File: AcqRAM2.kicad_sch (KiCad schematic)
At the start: 17 parts, among them U30 MSM5416283, U31 MSM5416283, U32 MSM5416283, U33 MSM5416283, U39 MSM5416283, U40 MSM5416283, U41 MSM5416283, U42 MSM5416283, U43 MSM5416283, U50 MSM5416283, U51 MSM5416283, U52 MSM5416283, U53 MSM5416283, U58 MSM5416283, U59 MSM5416283, U60 MSM5416283, U61 MSM5416283

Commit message: complete outer layers
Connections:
- net VSC13: now reaches U60.64 (SC)
- net VSC13: now also U52.64 (SC)
- net VSC12: now reaches U41.64 (SC)
- net VSC12: now also U31.64 (SC)
- net VSC9: now reaches U50.64 (SC)
- net VSC9: now also U58.64 (SC)
- net VSC10: now reaches U51.64 (SC)
- net VSC10: now also U59.64 (SC)
- net VSC17: now reaches U39.64 (SC)
- net VSC16: now reaches U43.64 (SC)
- net VSC16: now also U33.64 (SC)
- net VSC15: now reaches U42.64 (SC)
- net VSC15: now also U32.64 (SC)
- net VSC14: now reaches U53.64 (SC)
- net VSC14: now also U61.64 (SC)
- net VSC11: now reaches U30.64 (SC)
- net VSC11: now also U40.64 (SC)
- no-connect marks 0 -> 16
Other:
- note removed: "all chips"

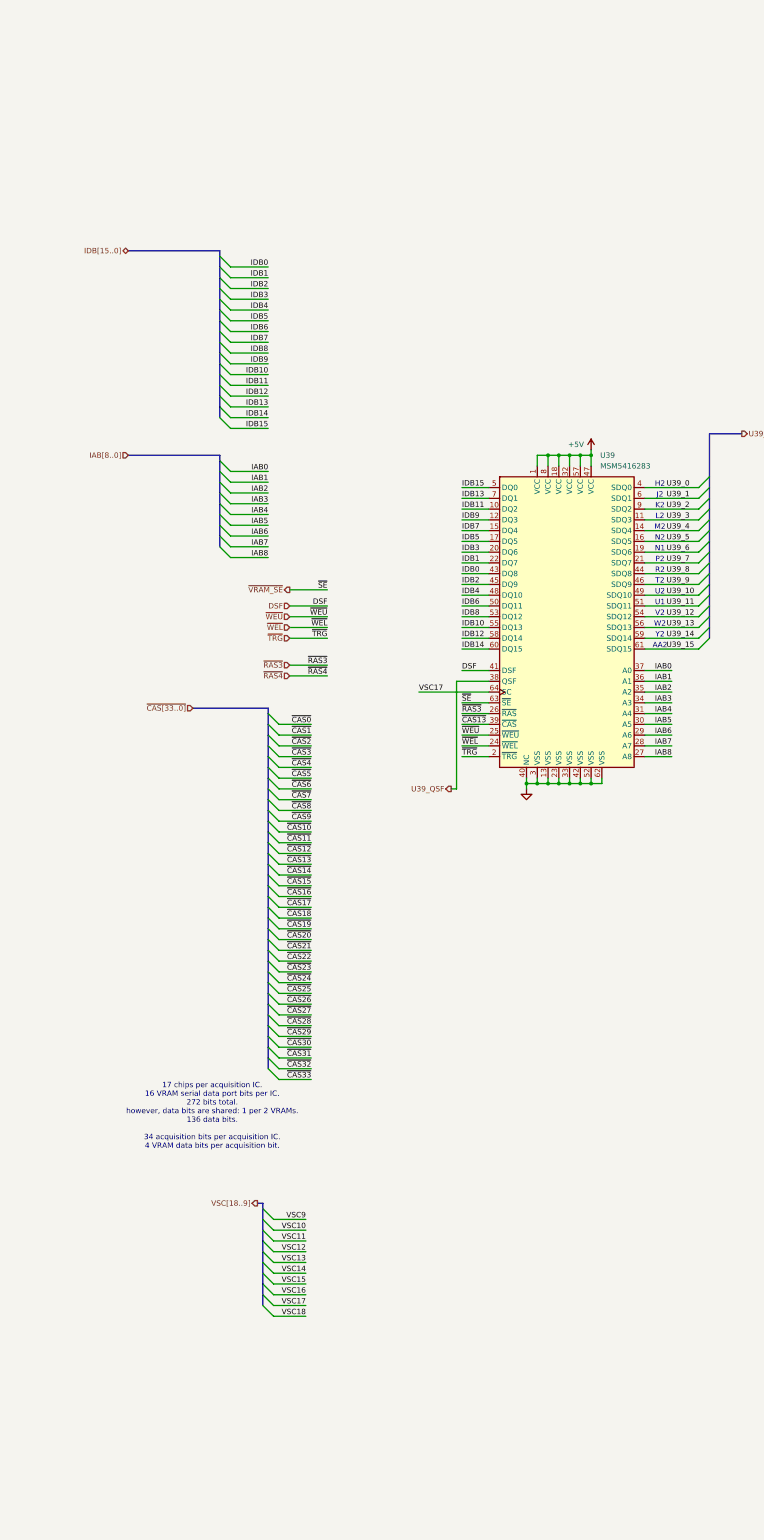
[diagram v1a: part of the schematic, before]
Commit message: add test points
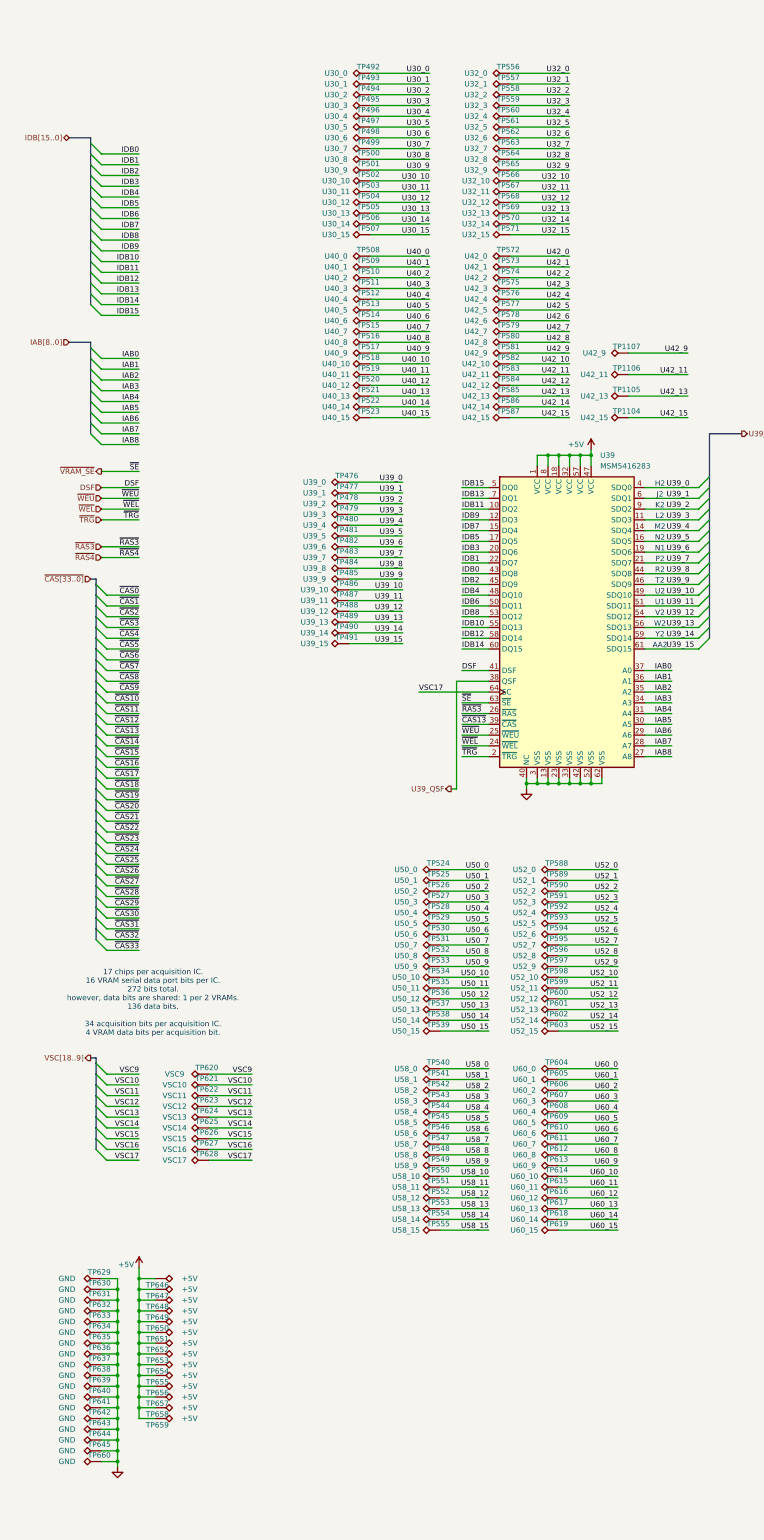
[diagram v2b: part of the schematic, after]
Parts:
- added TP1104, TP587: U42_15, hp16717:HP_TP30, symbol Connector:TestPoint_Alt
- added TP1105, TP585: U42_13, hp16717:HP_TP30, symbol Connector:TestPoint_Alt
- added TP1106, TP583: U42_11, hp16717:HP_TP30, symbol Connector:TestPoint_Alt
- added TP1107, TP581: U42_9, hp16717:HP_TP30, symbol Connector:TestPoint_Alt
- added TP476: U39_0, hp16717:HP_TP30, symbol Connector:TestPoint_Alt
- added TP477: U39_1, hp16717:HP_TP30, symbol Connector:TestPoint_Alt
- added TP478: U39_2, hp16717:HP_TP30, symbol Connector:TestPoint_Alt
- added TP479: U39_3, hp16717:HP_TP30, symbol Connector:TestPoint_Alt
- added TP480: U39_4, hp16717:HP_TP30, symbol Connector:TestPoint_Alt
- added TP481: U39_5, hp16717:HP_TP30, symbol Connector:TestPoint_Alt
- added TP482: U39_6, hp16717:HP_TP30, symbol Connector:TestPoint_Alt
- added TP483: U39_7, hp16717:HP_TP30, symbol Connector:TestPoint_Alt
- added TP484: U39_8, hp16717:HP_TP30, symbol Connector:TestPoint_Alt
- added TP485: U39_9, hp16717:HP_TP30, symbol Connector:TestPoint_Alt
- added TP486: U39_10, hp16717:HP_TP30, symbol Connector:TestPoint_Alt
- added TP487: U39_11, hp16717:HP_TP30, symbol Connector:TestPoint_Alt
- added TP488: U39_12, hp16717:HP_TP30, symbol Connector:TestPoint_Alt
- added TP489: U39_13, hp16717:HP_TP30, symbol Connector:TestPoint_Alt
- added TP490: U39_14, hp16717:HP_TP30, symbol Connector:TestPoint_Alt
- added TP491: U39_15, hp16717:HP_TP30, symbol Connector:TestPoint_Alt
- added TP492: U30_0, hp16717:HP_TP30, symbol Connector:TestPoint_Alt
- added TP493: U30_1, hp16717:HP_TP30, symbol Connector:TestPoint_Alt
- added TP494: U30_2, hp16717:HP_TP30, symbol Connector:TestPoint_Alt
- added TP495: U30_3, hp16717:HP_TP30, symbol Connector:TestPoint_Alt
- added TP496: U30_4, hp16717:HP_TP30, symbol Connector:TestPoint_Alt
- added TP497: U30_5, hp16717:HP_TP30, symbol Connector:TestPoint_Alt
- added TP498: U30_6, hp16717:HP_TP30, symbol Connector:TestPoint_Alt
- added TP499: U30_7, hp16717:HP_TP30, symbol Connector:TestPoint_Alt
- added TP500: U30_8, hp16717:HP_TP30, symbol Connector:TestPoint_Alt
- added TP501: U30_9, hp16717:HP_TP30, symbol Connector:TestPoint_Alt
- added TP502: U30_10, hp16717:HP_TP30, symbol Connector:TestPoint_Alt
- added TP503: U30_11, hp16717:HP_TP30, symbol Connector:TestPoint_Alt
- added TP504: U30_12, hp16717:HP_TP30, symbol Connector:TestPoint_Alt
- added TP505: U30_13, hp16717:HP_TP30, symbol Connector:TestPoint_Alt
- added TP506: U30_14, hp16717:HP_TP30, symbol Connector:TestPoint_Alt
- added TP507: U30_15, hp16717:HP_TP30, symbol Connector:TestPoint_Alt
- added TP508: U40_0, hp16717:HP_TP30, symbol Connector:TestPoint_Alt
- added TP509: U40_1, hp16717:HP_TP30, symbol Connector:TestPoint_Alt
- added TP510: U40_2, hp16717:HP_TP30, symbol Connector:TestPoint_Alt
- added TP511: U40_3, hp16717:HP_TP30, symbol Connector:TestPoint_Alt
- added TP512: U40_4, hp16717:HP_TP30, symbol Connector:TestPoint_Alt
- added TP513: U40_5, hp16717:HP_TP30, symbol Connector:TestPoint_Alt
- added TP514: U40_6, hp16717:HP_TP30, symbol Connector:TestPoint_Alt
- added TP515: U40_7, hp16717:HP_TP30, symbol Connector:TestPoint_Alt
- added TP516: U40_8, hp16717:HP_TP30, symbol Connector:TestPoint_Alt
- added TP517: U40_9, hp16717:HP_TP30, symbol Connector:TestPoint_Alt
- added TP518: U40_10, hp16717:HP_TP30, symbol Connector:TestPoint_Alt
- added TP519: U40_11, hp16717:HP_TP30, symbol Connector:TestPoint_Alt
- added TP520: U40_12, hp16717:HP_TP30, symbol Connector:TestPoint_Alt
- added TP521: U40_13, hp16717:HP_TP30, symbol Connector:TestPoint_Alt
- added TP522: U40_14, hp16717:HP_TP30, symbol Connector:TestPoint_Alt
- added TP523: U40_15, hp16717:HP_TP30, symbol Connector:TestPoint_Alt
- added TP524: U50_0, hp16717:HP_TP30, symbol Connector:TestPoint_Alt
- added TP525: U50_1, hp16717:HP_TP30, symbol Connector:TestPoint_Alt
- added TP526: U50_2, hp16717:HP_TP30, symbol Connector:TestPoint_Alt
- added TP527: U50_3, hp16717:HP_TP30, symbol Connector:TestPoint_Alt
- added TP528: U50_4, hp16717:HP_TP30, symbol Connector:TestPoint_Alt
- added TP529: U50_5, hp16717:HP_TP30, symbol Connector:TestPoint_Alt
- added TP530: U50_6, hp16717:HP_TP30, symbol Connector:TestPoint_Alt
- added TP531: U50_7, hp16717:HP_TP30, symbol Connector:TestPoint_Alt
- added TP532: U50_8, hp16717:HP_TP30, symbol Connector:TestPoint_Alt
- added TP533: U50_9, hp16717:HP_TP30, symbol Connector:TestPoint_Alt
- added TP534: U50_10, hp16717:HP_TP30, symbol Connector:TestPoint_Alt
- added TP535: U50_11, hp16717:HP_TP30, symbol Connector:TestPoint_Alt
- added TP536: U50_12, hp16717:HP_TP30, symbol Connector:TestPoint_Alt
- added TP537: U50_13, hp16717:HP_TP30, symbol Connector:TestPoint_Alt
- added TP538: U50_14, hp16717:HP_TP30, symbol Connector:TestPoint_Alt
- added TP539: U50_15, hp16717:HP_TP30, symbol Connector:TestPoint_Alt
- added TP540: U58_0, hp16717:HP_TP30, symbol Connector:TestPoint_Alt
- added TP541: U58_1, hp16717:HP_TP30, symbol Connector:TestPoint_Alt
- added TP542: U58_2, hp16717:HP_TP30, symbol Connector:TestPoint_Alt
- added TP543: U58_3, hp16717:HP_TP30, symbol Connector:TestPoint_Alt
- added TP544: U58_4, hp16717:HP_TP30, symbol Connector:TestPoint_Alt
- added TP545: U58_5, hp16717:HP_TP30, symbol Connector:TestPoint_Alt
- added TP546: U58_6, hp16717:HP_TP30, symbol Connector:TestPoint_Alt
- added TP547: U58_7, hp16717:HP_TP30, symbol Connector:TestPoint_Alt
- added TP548: U58_8, hp16717:HP_TP30, symbol Connector:TestPoint_Alt
- added TP549: U58_9, hp16717:HP_TP30, symbol Connector:TestPoint_Alt
- added TP550: U58_10, hp16717:HP_TP30, symbol Connector:TestPoint_Alt
- added TP551: U58_11, hp16717:HP_TP30, symbol Connector:TestPoint_Alt
- added TP552: U58_12, hp16717:HP_TP30, symbol Connector:TestPoint_Alt
- added TP553: U58_13, hp16717:HP_TP30, symbol Connector:TestPoint_Alt
- added TP554: U58_14, hp16717:HP_TP30, symbol Connector:TestPoint_Alt
- added TP555: U58_15, hp16717:HP_TP30, symbol Connector:TestPoint_Alt
- added TP556: U32_0, hp16717:HP_TP30, symbol Connector:TestPoint_Alt
- added TP557: U32_1, hp16717:HP_TP30, symbol Connector:TestPoint_Alt
- added TP558: U32_2, hp16717:HP_TP30, symbol Connector:TestPoint_Alt
- added TP559: U32_3, hp16717:HP_TP30, symbol Connector:TestPoint_Alt
- added TP560: U32_4, hp16717:HP_TP30, symbol Connector:TestPoint_Alt
- added TP561: U32_5, hp16717:HP_TP30, symbol Connector:TestPoint_Alt
- added TP562: U32_6, hp16717:HP_TP30, symbol Connector:TestPoint_Alt
- added TP563: U32_7, hp16717:HP_TP30, symbol Connector:TestPoint_Alt
- added TP564: U32_8, hp16717:HP_TP30, symbol Connector:TestPoint_Alt
- added TP565: U32_9, hp16717:HP_TP30, symbol Connector:TestPoint_Alt
- added TP566: U32_10, hp16717:HP_TP30, symbol Connector:TestPoint_Alt
- added TP567: U32_11, hp16717:HP_TP30, symbol Connector:TestPoint_Alt
- added TP568: U32_12, hp16717:HP_TP30, symbol Connector:TestPoint_Alt
- added TP569: U32_13, hp16717:HP_TP30, symbol Connector:TestPoint_Alt
- added TP570: U32_14, hp16717:HP_TP30, symbol Connector:TestPoint_Alt
- added TP571: U32_15, hp16717:HP_TP30, symbol Connector:TestPoint_Alt
- added TP572: U42_0, hp16717:HP_TP30, symbol Connector:TestPoint_Alt
- added TP573: U42_1, hp16717:HP_TP30, symbol Connector:TestPoint_Alt
- added TP574: U42_2, hp16717:HP_TP30, symbol Connector:TestPoint_Alt
- added TP575: U42_3, hp16717:HP_TP30, symbol Connector:TestPoint_Alt
- added TP576: U42_4, hp16717:HP_TP30, symbol Connector:TestPoint_Alt
- added TP577: U42_5, hp16717:HP_TP30, symbol Connector:TestPoint_Alt
- added TP578: U42_6, hp16717:HP_TP30, symbol Connector:TestPoint_Alt
- added TP579: U42_7, hp16717:HP_TP30, symbol Connector:TestPoint_Alt
- added TP580: U42_8, hp16717:HP_TP30, symbol Connector:TestPoint_Alt
- added TP582: U42_10, hp16717:HP_TP30, symbol Connector:TestPoint_Alt
- added TP584: U42_12, hp16717:HP_TP30, symbol Connector:TestPoint_Alt
- added TP586: U42_14, hp16717:HP_TP30, symbol Connector:TestPoint_Alt
- added TP588: U52_0, hp16717:HP_TP30, symbol Connector:TestPoint_Alt
- added TP589: U52_1, hp16717:HP_TP30, symbol Connector:TestPoint_Alt
- added TP590: U52_2, hp16717:HP_TP30, symbol Connector:TestPoint_Alt
- added TP591: U52_3, hp16717:HP_TP30, symbol Connector:TestPoint_Alt
- added TP592: U52_4, hp16717:HP_TP30, symbol Connector:TestPoint_Alt
- added TP593: U52_5, hp16717:HP_TP30, symbol Connector:TestPoint_Alt
- added TP594: U52_6, hp16717:HP_TP30, symbol Connector:TestPoint_Alt
- added TP595: U52_7, hp16717:HP_TP30, symbol Connector:TestPoint_Alt
- added TP596: U52_8, hp16717:HP_TP30, symbol Connector:TestPoint_Alt
- added TP597: U52_9, hp16717:HP_TP30, symbol Connector:TestPoint_Alt
- added TP598: U52_10, hp16717:HP_TP30, symbol Connector:TestPoint_Alt
- added TP599: U52_11, hp16717:HP_TP30, symbol Connector:TestPoint_Alt
- added TP600: U52_12, hp16717:HP_TP30, symbol Connector:TestPoint_Alt
- added TP601: U52_13, hp16717:HP_TP30, symbol Connector:TestPoint_Alt
- added TP602: U52_14, hp16717:HP_TP30, symbol Connector:TestPoint_Alt
- added TP603: U52_15, hp16717:HP_TP30, symbol Connector:TestPoint_Alt
- added TP604: U60_0, hp16717:HP_TP30, symbol Connector:TestPoint_Alt
- added TP605: U60_1, hp16717:HP_TP30, symbol Connector:TestPoint_Alt
- added TP606: U60_2, hp16717:HP_TP30, symbol Connector:TestPoint_Alt
- added TP607: U60_3, hp16717:HP_TP30, symbol Connector:TestPoint_Alt
- added TP608: U60_4, hp16717:HP_TP30, symbol Connector:TestPoint_Alt
- added TP609: U60_5, hp16717:HP_TP30, symbol Connector:TestPoint_Alt
- added TP610: U60_6, hp16717:HP_TP30, symbol Connector:TestPoint_Alt
- added TP611: U60_7, hp16717:HP_TP30, symbol Connector:TestPoint_Alt
- added TP612: U60_8, hp16717:HP_TP30, symbol Connector:TestPoint_Alt
- added TP613: U60_9, hp16717:HP_TP30, symbol Connector:TestPoint_Alt
- added TP614: U60_10, hp16717:HP_TP30, symbol Connector:TestPoint_Alt
- added TP615: U60_11, hp16717:HP_TP30, symbol Connector:TestPoint_Alt
- added TP616: U60_12, hp16717:HP_TP30, symbol Connector:TestPoint_Alt
- added TP617: U60_13, hp16717:HP_TP30, symbol Connector:TestPoint_Alt
- added TP618: U60_14, hp16717:HP_TP30, symbol Connector:TestPoint_Alt
- added TP619: U60_15, hp16717:HP_TP30, symbol Connector:TestPoint_Alt
- added TP620: VSC9, hp16717:HP_TP30, symbol Connector:TestPoint_Alt
- added TP621: VSC10, hp16717:HP_TP30, symbol Connector:TestPoint_Alt
- added TP622: VSC11, hp16717:HP_TP30, symbol Connector:TestPoint_Alt
- added TP623: VSC12, hp16717:HP_TP30, symbol Connector:TestPoint_Alt
- added TP624: VSC13, hp16717:HP_TP30, symbol Connector:TestPoint_Alt
- added TP625: VSC14, hp16717:HP_TP30, symbol Connector:TestPoint_Alt
- added TP626: VSC15, hp16717:HP_TP30, symbol Connector:TestPoint_Alt
- added TP627: VSC16, hp16717:HP_TP30, symbol Connector:TestPoint_Alt
- added TP628: VSC17, hp16717:HP_TP30, symbol Connector:TestPoint_Alt
- added TP629, TP630, TP631, TP632, TP633, TP634, TP635, TP636, TP637, TP638, TP639, TP640, TP641, TP642, TP643, TP644, TP645, TP660: GND, hp16717:HP_TP30, symbol Connector:TestPoint_Alt
- added TP646, TP647, TP648, TP649, TP650, TP651, TP652, TP653, TP654, TP655, TP656, TP657, TP658, TP659: +5V, hp16717:HP_TP30, symbol Connector:TestPoint_Alt
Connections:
- net +5V: now also TP646.1, TP647.1, TP648.1, TP649.1, TP650.1, TP651.1, TP652.1, TP653.1, TP654.1, TP655.1, TP656.1, TP657.1, TP658.1, TP659.1
- net GND: now also TP629.1, TP630.1, TP631.1, TP632.1, TP633.1, TP634.1, TP635.1, TP636.1, TP637.1, TP638.1, TP639.1, TP640.1, TP641.1, TP642.1, TP643.1, TP644.1, TP645.1, TP660.1
- net U30_0: now also TP492.1
- net U30_1: now also TP493.1
- net U30_10: now also TP502.1
- net U30_11: now also TP503.1
- net U30_12: now also TP504.1
- net U30_13: now also TP505.1
- net U30_14: now also TP506.1
- net U30_15: now also TP507.1
- net U30_2: now also TP494.1
- net U30_3: now also TP495.1
- net U30_4: now also TP496.1
- net U30_5: now also TP497.1
- net U30_6: now also TP498.1
- net U30_7: now also TP499.1
- net U30_8: now also TP500.1
- net U30_9: now also TP501.1
- net U32_0: now also TP556.1
- net U32_1: now also TP557.1
- net U32_10: now also TP566.1
- net U32_11: now also TP567.1
- net U32_12: now also TP568.1
- net U32_13: now also TP569.1
- net U32_14: now also TP570.1
- net U32_15: now also TP571.1
- net U32_2: now also TP558.1
- net U32_3: now also TP559.1
- net U32_4: now also TP560.1
- net U32_5: now also TP561.1
- net U32_6: now also TP562.1
- net U32_7: now also TP563.1
- net U32_8: now also TP564.1
- net U32_9: now also TP565.1
- net U39_0: now also TP476.1
- net U39_1: now also TP477.1
- net U39_10: now also TP486.1
- net U39_11: now also TP487.1
- net U39_12: now also TP488.1
- net U39_13: now also TP489.1
- net U39_14: now also TP490.1
- net U39_15: now also TP491.1
- net U39_2: now also TP478.1
- net U39_3: now also TP479.1
- net U39_4: now also TP480.1
- net U39_5: now also TP481.1
- net U39_6: now also TP482.1
- net U39_7: now also TP483.1
- net U39_8: now also TP484.1
- net U39_9: now also TP485.1
- net U40_0: now also TP508.1
- net U40_1: now also TP509.1
- net U40_10: now also TP518.1
- net U40_11: now also TP519.1
- net U40_12: now also TP520.1
- net U40_13: now also TP521.1
- net U40_14: now also TP522.1
- net U40_15: now also TP523.1
- net U40_2: now also TP510.1
- net U40_3: now also TP511.1
- net U40_4: now also TP512.1
- net U40_5: now also TP513.1
- net U40_6: now also TP514.1
- net U40_7: now also TP515.1
- net U40_8: now also TP516.1
- net U40_9: now also TP517.1
- net U42_0: now also TP572.1
- net U42_1: now also TP573.1
- net U42_10: now also TP582.1
- net U42_11: now also TP1106.1, TP583.1
- net U42_12: now also TP584.1
- net U42_13: now also TP1105.1, TP585.1
- net U42_14: now also TP586.1
- net U42_15: now also TP1104.1, TP587.1
- net U42_2: now also TP574.1
- net U42_3: now also TP575.1
- net U42_4: now also TP576.1
- net U42_5: now also TP577.1
- net U42_6: now also TP578.1
- net U42_7: now also TP579.1
- net U42_8: now also TP580.1
- net U42_9: now also TP1107.1, TP581.1
- net U50_0: now also TP524.1
- net U50_1: now also TP525.1
- net U50_10: now also TP534.1
- net U50_11: now also TP535.1
- net U50_12: now also TP536.1
- net U50_13: now also TP537.1
- net U50_14: now also TP538.1
- net U50_15: now also TP539.1
- net U50_2: now also TP526.1
- net U50_3: now also TP527.1
- net U50_4: now also TP528.1
- net U50_5: now also TP529.1
- net U50_6: now also TP530.1
- net U50_7: now also TP531.1
- net U50_8: now also TP532.1
- net U50_9: now also TP533.1
- net U52_0: now also TP588.1
- net U52_1: now also TP589.1
- net U52_10: now also TP598.1
- net U52_11: now also TP599.1
- net U52_12: now also TP600.1
- net U52_13: now also TP601.1
- net U52_14: now also TP602.1
- net U52_15: now also TP603.1
- net U52_2: now also TP590.1
- net U52_3: now also TP591.1
- net U52_4: now also TP592.1
- net U52_5: now also TP593.1
- net U52_6: now also TP594.1
- net U52_7: now also TP595.1
- net U52_8: now also TP596.1
- net U52_9: now also TP597.1
- net U58_0: now also TP540.1
- net U58_1: now also TP541.1
- net U58_10: now also TP550.1
- net U58_11: now also TP551.1
- net U58_12: now also TP552.1
- net U58_13: now also TP553.1
- net U58_14: now also TP554.1
- net U58_15: now also TP555.1
- net U58_2: now also TP542.1
- net U58_3: now also TP543.1
- net U58_4: now also TP544.1
- net U58_5: now also TP545.1
- net U58_6: now also TP546.1
- net U58_7: now also TP547.1
- net U58_8: now also TP548.1
- net U58_9: now also TP549.1
- net U60_0: now also TP604.1
- net U60_1: now also TP605.1
- net U60_10: now also TP614.1
- net U60_11: now also TP615.1
- net U60_12: now also TP616.1
- net U60_13: now also TP617.1
- net U60_14: now also TP618.1
- net U60_15: now also TP619.1
- net U60_2: now also TP606.1
- net U60_3: now also TP607.1
- net U60_4: now also TP608.1
- net U60_5: now also TP609.1
- net U60_6: now also TP610.1
- net U60_7: now also TP611.1
- net U60_8: now also TP612.1
- net U60_9: now also TP613.1
- net VSC10: now also TP621.1
- net VSC11: now also TP622.1
- net VSC12: now also TP623.1
- net VSC13: now also TP624.1
- net VSC14: now also TP625.1
- net VSC15: now also TP626.1
- net VSC16: now also TP627.1
- net VSC17: now also TP628.1
- net VSC9: now also TP620.1
